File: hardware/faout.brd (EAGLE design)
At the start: 100 x 70 mm, 165 parts, among them IC2 MT48LC8M16A2, Q1 12MHz, Q2 MUN2214T1, Q3 MUN2214T1, Q4 ASFL, SW1 SMD_TACT_SWITCH, SW2 SMD_TACT_SWITCH, SW3 SMD_TACT_SWITCH, U1 93LC46BT-I/OT, U10 REF102AU, U11 DAC8811DGK, U12 REF102AU, U13 DAC8811DGK, U14 ADR435ARZ, U15 AD8627AKSZ-R2, U16 OPA2277UA/2K5E4, U17 OPA2277UA/2K5E4, U18 MCP1700T-2502E/TT, U19 AD7980ARMZ, U2 LM3480IM3-3.3, U3 L7812ACV, U4 L7912ACV, U5 LM3671MF-3.3, U6 LM3671MF-1.2, U7 M25PE16, U8 6SLX9TQG144, U9 AD8220ARMZ

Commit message: Fix DAC voltage ref oscillations in next board version.
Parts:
- added C87, C88: 1uF, faout:R0603
- C67, C69: value 1uF? -> 1uF
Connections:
- new net N$17: C87.1, U10.8
- new net N$27: C88.1, U12.8
- net DAC1_VREF: no longer C67.2
- net DAC2_VREF: no longer C69.2
- net GND: now also C67.2, C69.2, C87.2, C88.2
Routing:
- net DAC1_VREF: track 22.4 -> 19.2 mm
- net DAC2_VREF: track 22.6 -> 19.4 mm
- net N$27: track 0.00 -> 2.78 mm
- net N$17: track 0.00 -> 2.78 mm
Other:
- board text added: "TU KL (06/2014)"
- board text removed: "TU KL (05/2014)"
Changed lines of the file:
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@@
 <layer number="27" name="tValues" color="7" fill="1" visible="no" active="yes"/>
 <layer number="28" name="bValues" color="7" fill="1" visible="no" active="yes"/>
-<layer number="29" name="tStop" color="7" fill="3" visible="yes" active="yes"/>
+<layer number="29" name="tStop" color="7" fill="3" visible="no" active="yes"/>
 <layer number="30" name="bStop" color="7" fill="6" visible="no" active="yes"/>
 <layer number="31" name="tCream" color="7" fill="4" visible="no" active="yes"/>
@@
 <text x="9.525" y="47.3075" size="1.4224" layer="25" ratio="12" align="top-left">FPGA - Analog In/Out
 Evaluation Board</text>
-<text x="9.525" y="42.8625" size="1.016" layer="25" ratio="12" align="top-left">TU KL (05/2014)</text>
+<text x="9.525" y="42.8625" size="1.016" layer="25" ratio="12" align="top-left">TU KL (06/2014)</text>
 </plain>
 <attributes>
@@
 </element>
 <element name="R29" library="faout" package="R0603" value="2k" x="78.4225" y="26.3525" smashed="yes" rot="R90">
-<attribute name="NAME" x="78.4225" y="24.4475" size="0.6096" layer="25" font="vector" ratio="14" rot="R270" align="center-left"/>
+<attribute name="NAME" x="77.1525" y="27.305" size="0.6096" layer="25" font="vector" ratio="14" rot="R270" align="center-left"/>
 <attribute name="VALUE" x="79.0575" y="28.2575" size="0.4064" layer="27" font="vector" ratio="14" rot="R90" align="center-left"/>
 </element>
-<element name="C67" library="faout" package="R0603" value="1uF?" x="87.9475" y="24.765" smashed="yes" rot="R90">
+<element name="C67" library="faout" package="R0603" value="1uF" x="87.9475" y="24.765" smashed="yes" rot="R90">
 <attribute name="NAME" x="87.9475" y="22.86" size="0.6096" layer="25" font="vector" ratio="14" rot="R270" align="center-left"/>
 <attribute name="VALUE" x="88.5825" y="26.67" size="0.4064" layer="27" font="vector" ratio="14" rot="R90" align="center-left"/>
@@
 </element>
 <element name="R30" library="faout" package="R0603" value="2k" x="78.4225" y="6.985" smashed="yes" rot="R90">
-<attribute name="NAME" x="78.4225" y="5.08" size="0.6096" layer="25" font="vector" ratio="14" rot="R270" align="center-left"/>
+<attribute name="NAME" x="77.1525" y="7.62" size="0.6096" layer="25" font="vector" ratio="14" rot="R270" align="center-left"/>
 <attribute name="VALUE" x="79.0575" y="8.89" size="0.4064" layer="27" font="vector" ratio="14" rot="R90" align="center-left"/>
 </element>
-<element name="C69" library="faout" package="R0603" value="1uF?" x="87.9475" y="5.3975" smashed="yes" rot="R90">
+<element name="C69" library="faout" package="R0603" value="1uF" x="87.9475" y="5.3975" smashed="yes" rot="R90">
 <attribute name="NAME" x="87.9475" y="3.4925" size="0.6096" layer="25" font="vector" ratio="14" rot="R270" align="center-left"/>
 <attribute name="VALUE" x="88.5825" y="7.3025" size="0.4064" layer="27" font="vector" ratio="14" rot="R90" align="center-left"/>
@@
 <attribute name="VALUE" x="53.0225" y="11.7475" size="0.4064" layer="27" font="vector" ratio="14" align="center-left"/>
 </element>
+<element name="C87" library="faout" package="R0603" value="1uF" x="78.4225" y="23.1775" smashed="yes" rot="R270">
+<attribute name="OC_FARNELL" value="1759409" x="78.4225" y="23.1775" size="1.778" layer="27" rot="R270" display="off"/>
+<attribute name="NAME" x="77.1525" y="24.13" size="0.6096" layer="25" font="vector" ratio="14" rot="R270" align="center-left"/>
+<attribute name="VALUE" x="77.7875" y="21.2725" size="0.4064" layer="27" font="vector" ratio="14" rot="R270" align="center-left"/>
+</element>
+<element name="C88" library="faout" package="R0603" value="1uF" x="78.4225" y="3.81" smashed="yes" rot="R270">
+<attribute name="OC_FARNELL" value="1759409" x="78.4225" y="3.81" size="1.778" layer="27" rot="R270" display="off"/>
+<attribute name="NAME" x="77.1525" y="4.7625" size="0.6096" layer="25" font="vector" ratio="14" rot="R270" align="center-left"/>
+<attribute name="VALUE" x="77.7875" y="1.905" size="0.4064" layer="27" font="vector" ratio="14" rot="R270" align="center-left"/>
+</element>
 </elements>
 <signals>
@@
 <contactref element="R7" pad="1"/>
 <contactref element="U7" pad="4"/>
+<contactref element="C67" pad="2"/>
+<contactref element="C87" pad="2"/>
+<contactref element="C69" pad="2"/>
+<contactref element="C88" pad="2"/>
 </signal>
 <signal name="USB_DM">
@@
 <contactref element="U10" pad="4"/>
 <contactref element="U11" pad="4"/>
-<contactref element="C67" pad="2"/>
 <contactref element="U17" pad="7"/>
 <contactref element="C78" pad="2"/>
@@
 <wire x1="85.4075" y1="27.305" x2="85.6488" y2="27.0637" width="0.4064" layer="1"/>
 <wire x1="85.6488" y1="26.67" x2="85.6488" y2="27.0637" width="0.4064" layer="1"/>
-<wire x1="85.6488" y1="26.67" x2="87.63" y2="26.67" width="0.4064" layer="1"/>
-<wire x1="87.63" y1="26.67" x2="87.9475" y2="26.3525" width="0.4064" layer="1"/>
-<wire x1="87.9475" y1="25.615" x2="87.9475" y2="26.3525" width="0.4064" layer="1"/>
 </signal>
 <signal name="!DAC1_CS">
@@
 <contactref element="C79" pad="2"/>
 <contactref element="U12" pad="4"/>
-<contactref element="C69" pad="2"/>
 <contactref element="U16" pad="7"/>
 <contactref element="U13" pad="4"/>
 <wire x1="80.7212" y1="11.7475" x2="78.6375" y2="11.7475" width="0.4064" layer="1"/>
 <wire x1="78.6375" y1="11.7475" x2="78.4225" y2="11.5325" width="0.4064" layer="1"/>
-<wire x1="85.6488" y1="7.3025" x2="87.63" y2="7.3025" width="0.4064" layer="1"/>
-<wire x1="87.63" y1="7.3025" x2="87.9475" y2="6.985" width="0.4064" layer="1"/>
-<wire x1="87.9475" y1="6.2475" x2="87.9475" y2="6.985" width="0.4064" layer="1"/>
 <wire x1="85.6488" y1="7.3025" x2="85.6488" y2="7.6962" width="0.4064" layer="1"/>
 <wire x1="85.6488" y1="7.6962" x2="85.4075" y2="7.9375" width="0.4064" layer="1"/>
@@
 <wire x1="87.9475" y1="21.9075" x2="86.995" y2="20.955" width="0.8128" layer="1"/>
 <wire x1="86.995" y1="20.955" x2="86.995" y2="18.63" width="0.8128" layer="1"/>
-<wire x1="76.835" y1="1.905" x2="76.835" y2="2.54" width="1.016" layer="16"/>
-<wire x1="76.835" y1="2.54" x2="76.835" y2="20.955" width="1.016" layer="16"/>
+<wire x1="76.835" y1="1.5875" x2="76.835" y2="2.2225" width="1.016" layer="16"/>
+<wire x1="76.835" y1="2.2225" x2="76.835" y2="20.955" width="1.016" layer="16"/>
 <wire x1="76.835" y1="20.955" x2="76.835" y2="21.59" width="1.016" layer="16"/>
 <wire x1="76.835" y1="21.59" x2="76.835" y2="39.6875" width="1.016" layer="16"/>
@@
 <wire x1="86.0425" y1="40.3225" x2="86.995" y2="39.37" width="0.8128" layer="1"/>
 <via x="76.835" y="20.955" extent="1-16" drill="0.3" alwaysstop="yes"/>
-<via x="76.835" y="1.905" extent="1-16" drill="0.3" alwaysstop="yes"/>
-<wire x1="76.835" y1="1.905" x2="87.3125" y2="1.905" width="0.8128" layer="1"/>
-<wire x1="87.3125" y1="1.905" x2="87.9475" y2="2.54" width="0.8128" layer="1"/>
-<wire x1="76.835" y1="1.905" x2="76.835" y2="2.54" width="0.8128" layer="1"/>
+<via x="76.835" y="1.5875" extent="1-16" drill="0.3" alwaysstop="yes"/>
+<wire x1="76.835" y1="1.5875" x2="86.995" y2="1.5875" width="0.8128" layer="1"/>
+<wire x1="86.995" y1="1.5875" x2="87.9475" y2="2.54" width="0.8128" layer="1"/>
+<wire x1="76.835" y1="1.5875" x2="76.835" y2="2.2225" width="0.8128" layer="1"/>
 <wire x1="76.835" y1="20.955" x2="76.835" y2="21.59" width="0.8128" layer="1"/>
 <wire x1="76.835" y1="40.3225" x2="76.835" y2="39.6875" width="0.8128" layer="1"/>
 <via x="76.835" y="39.6875" extent="1-16" drill="0.3" alwaysstop="yes"/>
 <via x="76.835" y="21.59" extent="1-16" drill="0.3" alwaysstop="yes"/>
-<via x="76.835" y="2.54" extent="1-16" drill="0.3" alwaysstop="yes"/>
+<via x="76.835" y="2.2225" extent="1-16" drill="0.3" alwaysstop="yes"/>
 <contactref element="U18" pad="3"/>
 <contactref element="C86" pad="1"/>
@@
 <wire x1="18.835" y1="52.27" x2="18.635" y2="52.07" width="0.6096" layer="1"/>
 </signal>
+<signal name="N$17">
+<contactref element="U10" pad="8"/>
+<contactref element="C87" pad="1"/>
+<wire x1="80.7212" y1="22.86" x2="79.6925" y2="22.86" width="0.4064" layer="1"/>
+<wire x1="79.6925" y1="22.86" x2="78.525" y2="24.0275" width="0.4064" layer="1"/>
+<wire x1="78.4225" y1="24.0275" x2="78.525" y2="24.0275" width="0.4064" layer="1"/>
+</signal>
+<signal name="N$27">
+<contactref element="U12" pad="8"/>
+<contactref element="C88" pad="1"/>
+<wire x1="80.7212" y1="3.4925" x2="79.6925" y2="3.4925" width="0.4064" layer="1"/>
+<wire x1="78.4225" y1="4.66" x2="78.525" y2="4.66" width="0.4064" layer="1"/>
+<wire x1="78.525" y1="4.66" x2="79.6925" y2="3.4925" width="0.4064" layer="1"/>
+</signal>
 </signals>

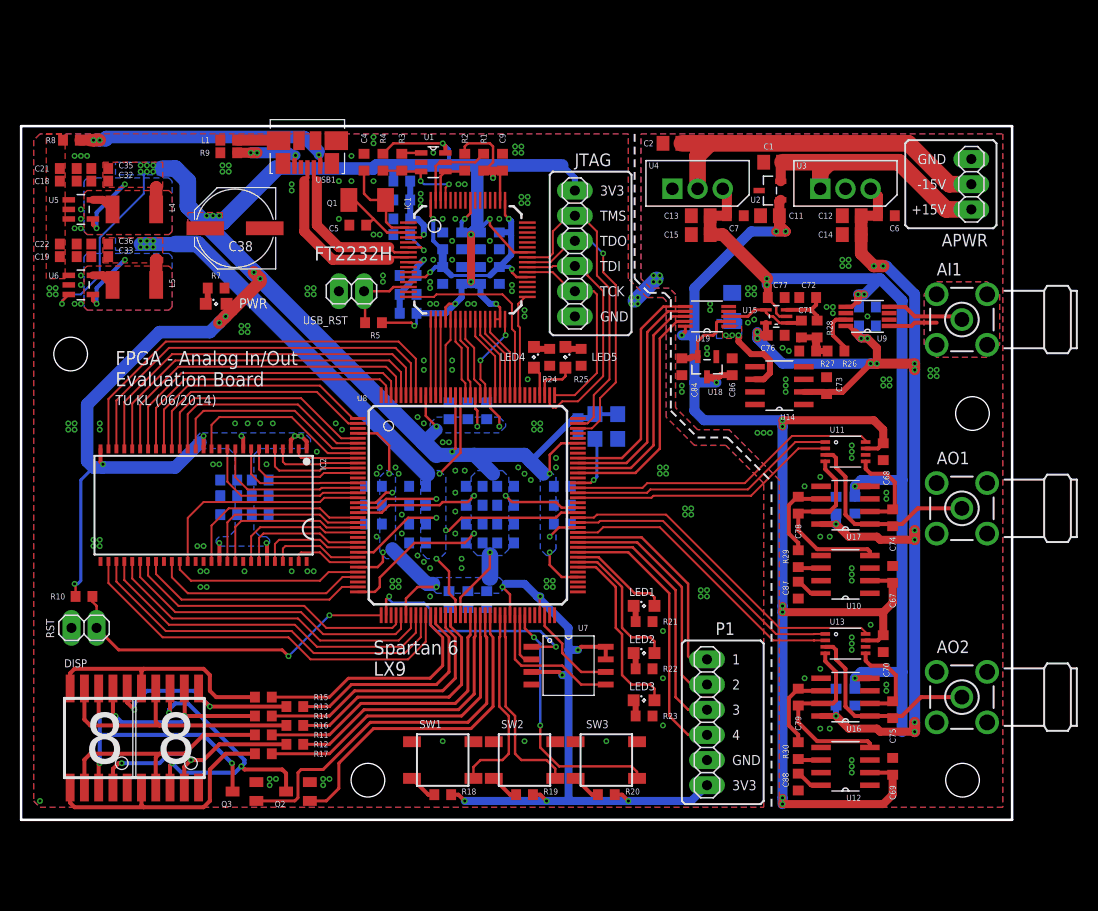
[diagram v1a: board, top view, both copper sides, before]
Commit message: Larger SMD pads and optional capacitors.
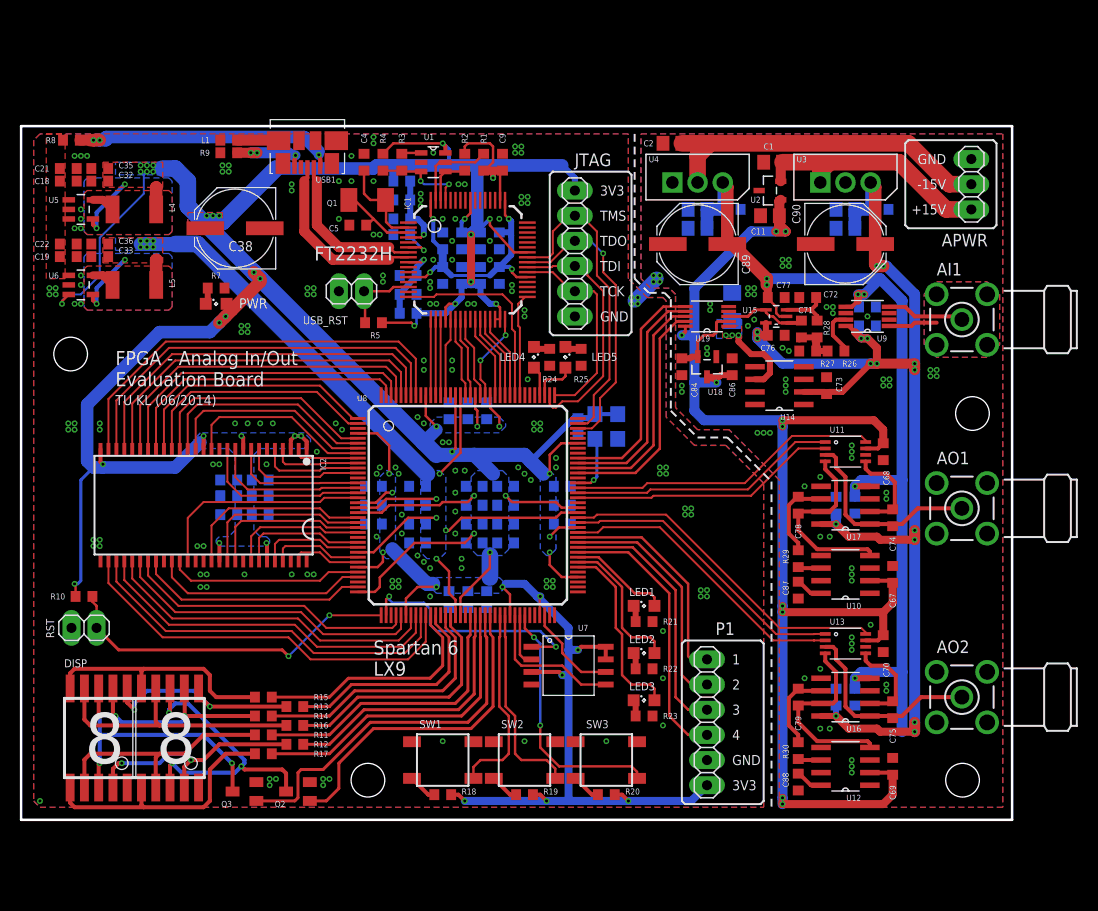
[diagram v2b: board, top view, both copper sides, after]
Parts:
- added C89, C90: 100uF, rcl:PANASONIC_E
- moved C6 0.90 mm to (86.7, 61.6), flipped to the bottom, turned to 180 degrees
- moved C12 0.90 mm to (83.2, 61.6), flipped to the bottom, turned to 0 degrees
- moved C14 0.90 mm to (83.2, 59.7), flipped to the bottom, turned to 0 degrees
- moved C7 0.71 mm to (71.8, 61.6), flipped to the bottom, turned to 0 degrees
- moved C13 0.71 mm to (68.3, 61.6), flipped to the bottom, turned to 180 degrees
- moved C15 0.71 mm to (68.3, 59.7), flipped to the bottom, turned to 180 degrees
- moved U3 0.64 mm to (85.7, 65.4)
- moved U4 0.64 mm to (70.8, 65.4)
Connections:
- net A+12V: now also C90.+
- net A-12V: now also C89.-
- net GND: now also C89.+, C90.-
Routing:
- net A-12V: track 99.9 -> 104.1 mm
- net A+12V: track 122.7 -> 126.8 mm
- net -15V: track 36.0 -> 35.4 mm
- net +15V: track 26.1 -> 25.5 mm

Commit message: WIP: Design 6channel FAOUT prototype.
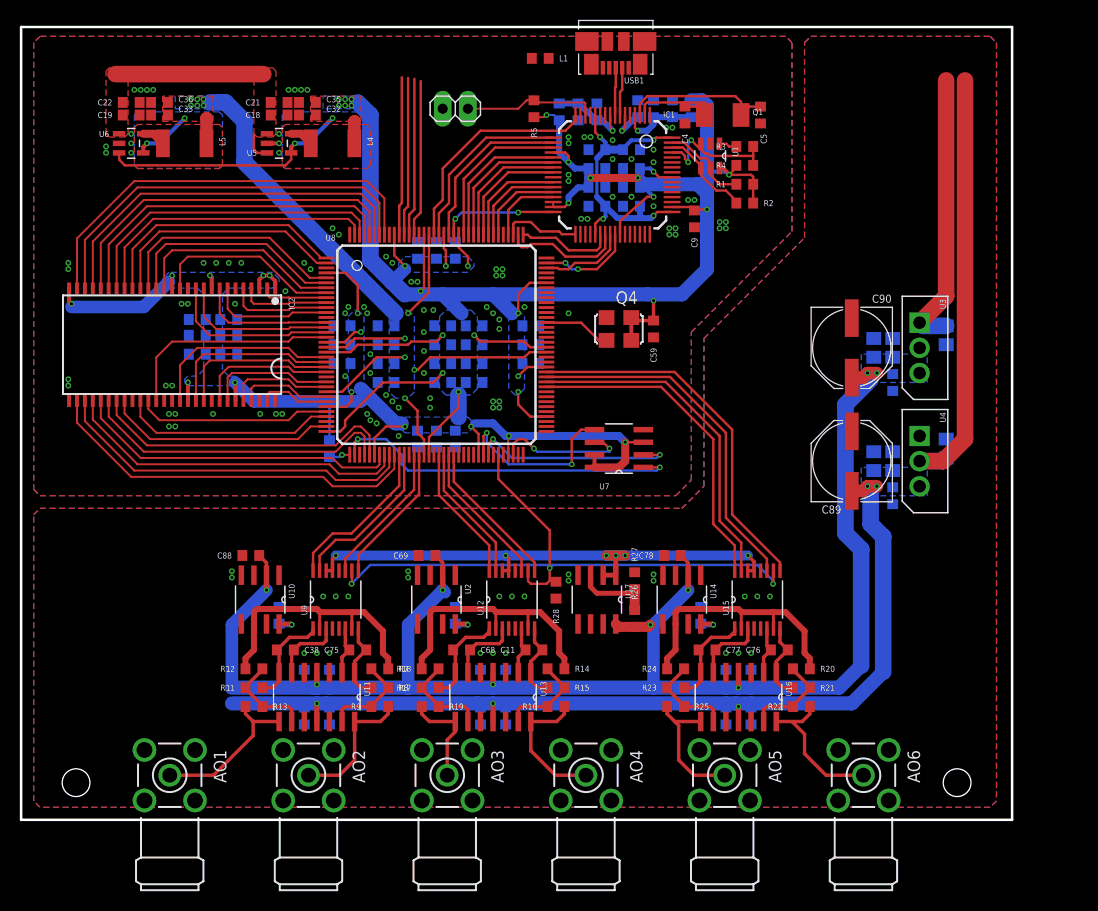
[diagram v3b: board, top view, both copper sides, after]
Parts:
- removed AI1: BU-SMA, analog_out_lib:BU-SMA-H
- removed APWR: (no value), pinhead:1X03
- removed C86, C87: 1uF, faout:R0603
- removed DISP: 7SEG_DISPLAY, faout:7SEG_DISPLAY
- removed JTAG, P1: (no value), pinhead:1X06
- removed LED1, LED2, LED3, LED4, LED5, PWR: (no value), led:SML0805
- removed Q2, Q3: MUN2214T1, transistor-npn:SC59-BEC
- removed R29, R30: 2k, faout:R0603
- removed RST: (no value), pinhead:1X02
- removed SW1, SW2, SW3: SMD_TACT_SWITCH, faout:SMD_TACT_SWITCH
- removed U18: MCP1700T-2502E/TT, faout:SOT95P264X112-3N
- removed U19: AD7980ARMZ, faout:SOP50P490X110-10N
- added AO3, AO4, AO5, AO6: BU-SMA, analog_out_lib:BU-SMA-H
- C11: value 10uF -> 20pF; device faout:R0805 -> faout:R0603
- C38: value 100uF -> 20pF; device rcl:PANASONIC_E -> faout:R0603
- C65, C66, C70, C73: value 100nF -> 1uF
- C68, C76, C77: value 100nF -> 20pF
- C71: value 114pF -> 100nF
- C72: value 11.4pF -> 100nF
- C74: value 20pF -> 1uF
- C78, C79: value 1nF -> 1uF
- C85: value 22uF -> 1uF; device faout:R1206 -> faout:R0603
- R11, R15, R17: value 100 -> 5k
- R12, R13, R14, R16: value 100 -> 10k
- R21, R23: value 300 -> 5k
- R22, R24, R25, R7: value 300 -> 10k
- R26: value 7.47k -> 13.181k
- R27: value 7.47k -> 5k
- R28: value 134k -> 10k
- R8: value 0 -> 5k
- R9: value 0 -> 10k
- U11, U13: value DAC8811DGK -> OPA4277UA; device faout:MSOP-8 -> faout:SOIC127P600X175-14N
- U12: value REF102AU -> DAC8812; device faout:SOIC127P600X175-8N -> faout:SOP65P640X120-16N
- U14: value ADR435ARZ -> REF102AU
- U15: value AD8627AKSZ-R2 -> DAC8812; device faout:SOT65P210X110-5N -> faout:SOP65P640X120-16N
- U16: value OPA2277UA/2K5E4 -> OPA4277UA; device faout:SOIC127P600X175-8N -> faout:SOIC127P600X175-14N
- U2: value LM3480IM3-3.3 -> REF102AU; device faout:SOT95P251X112-3N -> faout:SOIC127P600X175-8N
- U7: value M25PE16 -> M25PE16SO8N; device faout:SO8W -> faout:SOIC127P600X175-8N
- U9: value AD8220ARMZ -> DAC8812; device faout:SOP65P490X110-8N -> faout:SOP65P640X120-16N
- moved AO1 84.3 mm to (15.0, 4.50), turned to 270 degrees
- moved AO2 66.4 mm to (29.0, 4.50), turned to 270 degrees
- moved C65 66.2 mm to (26.0, 20.6), turned to 90 degrees
- moved C66 66.0 mm to (31.1, 14.3), turned to 90 degrees
- moved R8 63.4 mm to (36.2, 13.3)
- moved U9 60.8 mm to (31.8, 22.2), turned to 90 degrees
- moved C88 59.8 mm to (23.2, 26.7), turned to 180 degrees
- moved U10 59.1 mm to (24.1, 22.2), turned to 270 degrees
- moved U11 58.8 mm to (29.8, 12.4), turned to 270 degrees
- moved C67 58.6 mm to (31.1, 10.5), flipped to the bottom
- moved R9 57.9 mm to (36.2, 11.4), turned to 180 degrees
- moved C81 55.6 mm to (28.6, 10.5)
- moved C75 54.3 mm to (34.0, 17.1), turned to 180 degrees
- moved C80 53.7 mm to (28.6, 14.3)
- moved C72 53.6 mm to (46.4, 10.5), flipped to the bottom, turned to 90 degrees
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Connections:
- removed net 2V5: C84.1, U18.2, U19.2
- removed net ADC1_CNV: U19.6, U8.100
- removed net ADC1_REF: C85.1, U14.6, U19.1
- removed net ADC1_SCK: U19.8, U8.98
- removed net ADC1_SDI: U19.9, U8.97
- removed net ADC1_SDO: U19.7, U8.99
- removed net BUTTON1: SW1.1, U8.61
- removed net BUTTON2: SW2.1, U8.62
- removed net BUTTON3: SW3.1, U8.66
- removed net DAC1_IOUT: C74.2, U11.5, U17.2
- removed net DAC1_VOUT: AO1.1, C74.1, U11.3, U17.1
- removed net DAC1_VREFOUT: C78.1, R29.2, U17.6
- removed net DAC2_IOUT: C75.2, U13.5, U16.2
- removed net DAC2_VOUT: AO2.1, C75.1, U13.3, U16.1
- removed net DAC2_VREFOUT: C79.1, R30.2, U16.6
- removed net DISP_A: R14.2, U8.50
- removed net DISP_B: R13.2, U8.48
- removed net DISP_C: R12.2, U8.56
- removed net DISP_CAT1: DISP.18, DISP.3, Q3.C
- removed net DISP_CAT2: DISP.13, DISP.8, Q2.C
- removed net DISP_D: R11.2, U8.55
- removed net DISP_E: R17.2, U8.57
- removed net DISP_EN1: Q3.B, U8.58
- removed net DISP_EN2: Q2.B, U8.59
- removed net DISP_F: R16.2, U8.51
- removed net DISP_G: R15.2, U8.47
- removed net DISP_INT_A: DISP.12, DISP.17, R14.1
- removed net DISP_INT_B: DISP.11, DISP.16, R13.1
- removed net DISP_INT_C: DISP.4, DISP.9, R12.1
- removed net DISP_INT_D: DISP.2, DISP.7, R11.1
- removed net DISP_INT_E: DISP.1, DISP.6, R17.1
- removed net DISP_INT_F: DISP.14, DISP.19, R16.1
- removed net DISP_INT_G: DISP.15, DISP.20, R15.1
- removed net JP_1: P1.1, U8.84
- removed net JP_2: P1.2, U8.83
- removed net JP_3: P1.3, U8.82
- removed net JP_4: P1.4, U8.81
- removed net LED1: LED1.A, U8.80
- removed net LED2: LED2.A, U8.79
- removed net LED3: LED3.A, U8.78
- removed net LED_4: LED4.A, U8.112
- removed net LED_5: LED5.A, U8.111
- removed net N$15: C72.1, R28.2, U15.3
- removed net N$17: C87.1, U10.8
- removed net N$18: R18.1, SW1.2
- removed net N$19: R19.1, SW2.2
- removed net N$22: LED2.C, R22.2
- removed net N$23: LED3.C, R23.2
- removed net N$26: PWR.C, R7.2
- removed net N$27: C88.1, U12.8
- removed net N$3: LED4.C, R24.2
- new net !DAC1_LDAC: U8.48, U9.15
- new net !DAC2_LDAC: U12.15, U8.56
- new net !DAC3_CS: U15.11, U8.84
- new net !DAC3_LDAC: U15.15, U8.83
- new net !DACX_RS: R28.1, U12.10, U15.10, U8.67, U9.10
- new net AGND: AO1.2, AO1.3, AO1.4, AO1.5, AO2.2, AO2.3, AO2.4, AO2.5, AO3.2, AO3.3, AO3.4, AO3.5, AO4.2, AO4.3, AO4.4, AO4.5, AO5.2, AO5.3, AO5.4, AO5.5, AO6.2, AO6.3, AO6.4, AO6.5, C1.2, C12.2, C13.1, C14.2, C15.1, C2.2, C6.2, C65.2, C66.2, C67.1, C69.2, C7.1, C70.2, C71.2, C72.1, C73.2, C74.1, C78.2, C79.2, C80.2, C81.1, C82.2, C83.1, C84.2, C85.1, C88.2, C89.+, C90.-, R27.2, R28.2, U10.4, U11.10, U11.12, U11.3, U11.5, U12.12, U12.4, U12.5, U13.10, U13.12, U13.3, U13.5, U14.4, U15.12, U15.4, U15.5, U16.10, U16.12, U16.3, U16.5, U17.4, U2.4, U3.2, U4.1, U9.12, U9.4, U9.5
- new net DAC1_IOUTA: C38.2, U11.6, U9.3
- new net DAC1_IOUTB: C75.2, U11.2, U9.6
- new net DAC1_RFBA: C38.1, R11.1, U11.7, U9.1
- new net DAC1_RFBB: C75.1, R8.1, U11.1, U9.8
- new net DAC1_VOUTA: AO1.1, R13.1, U11.8
- new net DAC1_VOUTB: AO2.1, R9.1, U11.14
- new net DAC2_IOUTA: C68.2, U12.3, U13.6
- new net DAC2_IOUTB: C11.2, U12.6, U13.2
- new net DAC2_RFBA: C68.1, R17.1, U12.1, U13.7
- new net DAC2_RFBB: C11.1, R15.1, U12.8, U13.1
- new net DAC2_VOUTA: AO3.1, R19.1, U13.8
- new net DAC2_VOUTB: AO4.1, R16.1, U13.14
- new net DAC3_CLK: U15.16, U8.82
- new net DAC3_IOUTA: C77.2, U15.3, U16.6
- new net DAC3_IOUTB: C76.2, U15.6, U16.2
- new net DAC3_RFBA: C77.1, R23.1, U15.1, U16.7
- new net DAC3_RFBB: C76.1, R21.1, U15.8, U16.1
- new net DAC3_SDI: U15.9, U8.85
- new net DAC3_VOUTA: AO5.1, R25.1, U16.8
- new net DAC3_VOUTB: AO6.1, R22.1, U16.14
- new net DAC3_VREF: R20.2, R24.2, U14.6, U15.2, U15.7
- new net GPIO_0_0: U8.134
- new net GPIO_0_1: U8.133
- new net GPIO_0_2: U8.132
- new net GPIO_0_3: U8.131
- net !DAC1_CS: now also U8.50, U9.11; no longer U11.8, U8.94
- net !DAC2_CS: now also U12.11, U8.57; no longer U13.8, U8.88
- net !USB_OE: now also U8.111; no longer U8.116
- net !USB_RD: now also U8.114; no longer U8.119
- net !USB_RXF: now also U8.116; no longer U8.121
- net !USB_TXE: now also U8.115; no longer U8.120
- net !USB_WR: now also U8.112; no longer U8.118
- net +15V: no longer APWR.1, U2.2
- net -15V: no longer APWR.2
- net 3V3: no longer C38.+, JTAG.6, P1.6, PWR.A, R18.2, R19.2, R20.2
- net 5V0: no longer R8.1
- net A+12V: now also C66.1, C69.1, C71.1, C78.1, C84.1, C88.1, R26.1, U10.2, U11.4, U13.4, U16.4, U2.2; no longer C65.1, C76.1, U15.5, U16.8, U9.8
- net A+3V3: now also U12.13, U12.14, U15.13, U15.14, U17.1, U17.2, U9.13, U9.14; no longer C11.1, C67.1, C68.1, C69.1, C70.1, C86.1, U10.2, U11.7, U12.2, U13.7, U18.3, U19.10, U2.1
- net A-12V: now also C67.2, C72.2, C74.2, C85.2, U11.11, U13.11, U16.11; no longer C66.2, C77.2, U15.2, U16.4, U17.4, U9.5
- net DAC1_CLK: now also U8.47, U9.16; no longer U11.1, U8.93
- net DAC1_SDI: now also U8.51, U9.9; no longer U11.2, U8.92
- net DAC1_VREF: now also R12.2, R7.2, U10.6, U9.2, U9.7; no longer C78.2, U10.4, U11.4, U17.7
- net DAC2_CLK: now also U12.16, U8.55; no longer U13.1, U8.87
- net DAC2_SDI: now also U12.9, U8.58; no longer U13.2, U8.85
- net DAC2_VREF: now also R14.2, R18.2, U12.2, U12.7, U2.6; no longer C79.2, U12.4, U13.4, U16.7
- net GND: no longer AO1.2, AO1.3, AO1.4, AO1.5, AO2.2, AO2.3, AO2.4, AO2.5, APWR.3, C1.2, C11.2, C12.2, C13.1, C14.2, C15.1, C2.2, C38.-, C6.2, C65.2, C66.1, C67.2, C68.2, C69.2, C7.1, C70.2, C72.2, C73.2, C76.2, C77.1, C80.2, C81.1, C82.2, C83.1, C84.2, C85.2, C86.2, C87.2, C88.2, C89.+, C90.-, JTAG.1, P1.5, Q2.E, Q3.E, R21.1, R22.1, R23.1, R24.1, R25.1, R27.1, R7.1, R9.1, RST.2, SW1.3, SW1.4, SW2.3, SW2.4, SW3.3, SW3.4, U11.6, U13.6, U14.4, U16.3, U16.5, U17.3, U17.5, U18.1, U19.4, U19.5, U2.3, U3.2, U4.1, U9.6
- net N$10: now also R20.1, R21.2, R22.2, U16.13; no longer R29.1, U10.6
- net N$11: now also C70.1, U2.8; no longer AI1.2, AI1.3, AI1.4, AI1.5, U9.1
- net N$12: now also C79.1, U14.8; no longer C71.1, U15.1, U15.4, U19.3
- net N$13: now also R27.1, U17.3; no longer U9.7
- net N$14: now also R23.2, R24.1, R25.2, U16.9; no longer C71.2, R26.1, R27.2, R28.1
- net N$20: now also R17.2, R18.1, R19.2, U13.9; no longer R20.1, SW3.2
- net N$21: now also R14.1, R15.2, R16.2, U13.13; no longer LED1.C, R21.2
- net N$4: now also C65.1, U10.8; no longer LED5.C, R25.2
- net N$8: now also R11.2, R12.1, R13.2, U11.9; no longer R30.1, U12.6
- net N$9: now also R7.1, R8.2, R9.2, U11.13; no longer AI1.1, U9.4
- net RAM_A8: now also U8.40; no longer U8.41
- net RAM_A9: now also U8.41; no longer U8.40
- net RESET: no longer RST.1
- net TCK: no longer JTAG.2
- net TDI: no longer JTAG.3
- net TDO: no longer JTAG.4
- net TMS: no longer JTAG.5
- net USB_D0: now also U8.127; no longer U8.117
- net USB_D1: now also U8.126; no longer U8.134
- net USB_D2: now also U8.124; no longer U8.133
- net USB_D3: now also U8.121; no longer U8.132
- net USB_D4: now also U8.120; no longer U8.131
- net USB_D5: now also U8.119; no longer U8.127
- net USB_D6: now also U8.118; no longer U8.126
- net USB_D7: now also U8.117; no longer U8.124
- net USB_GND: no longer R9.2
- net USB_V: no longer R8.2
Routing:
- net 3V3: track 449.7 -> 344.1 mm, vias 55 -> 43
- net A+3V3: track 136.9 -> 53.7 mm, vias 10 -> 6
- net !DACX_RS: track 0.00 -> 66.5 mm, vias 0 -> 3
- net DISP_EN1: track 37.8 -> 0.00 mm
- net DAC3_SDI: track 0.00 -> 37.4 mm
- net !DAC3_CS: track 0.00 -> 36.1 mm
- net !DAC3_LDAC: track 0.00 -> 34.2 mm
- net DISP_EN2: track 33.2 -> 0.00 mm
- net DAC3_CLK: track 0.00 -> 33.2 mm
- net RESET: track 35.0 -> 2.14 mm, vias 2 -> 1
- net DISP_E: track 31.7 -> 0.00 mm
- net DISP_CAT2: track 30.7 -> 0.00 mm, vias 3 -> 0
- net DISP_D: track 29.4 -> 0.00 mm
- net A+12V: track 126.8 -> 155.8 mm, vias 16 -> 9
- net JP_4: track 27.9 -> 0.00 mm
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- added copper zone on layer 16, net A+12V
- added copper zone on layer 16, net A-12V
- added copper zone on layer 1, net AGND
- added copper zone on layer 16, net AGND
- removed copper zone on layer 1, net ADC1_REF
- removed copper zone on layer 16, net ADC1_REF
- removed copper zone on layer 1, net N$11
- removed copper zone on layer 16, net N$11
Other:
- board size 100 x 70 mm -> 100 x 80 mm
- board text removed: "+15V"
- board text removed: "-15V"
- board text removed: "1"
- board text removed: "2"
- board text removed: "3"
- board text removed: "3V3"
- board text removed: "4"
- board text removed: "FPGA - Analog In/Out Evaluation Board"
- board text removed: "FT2232H"
- board text removed: "GND"
- board text removed: "Spartan 6 LX9"
- board text removed: "TCK"
- board text removed: "TDI"
- board text removed: "TDO"
- board text removed: "TMS"
- board text removed: "TU KL (06/2014)"
